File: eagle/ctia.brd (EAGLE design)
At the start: 69.8 x 65.7 mm, 9 parts, among them IC1 IVC102UADAPTOR

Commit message: board/solid works
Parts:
- removed X1, X3, X4, X6: (no value), con-molex:KK-156-2
- removed X2: (no value), con-molex:KK-156-6
- added U$1: CTIA, ctia:CTIA
- added X5: (no value), con-subd:F09HP
- moved R2 22.2 mm to (36.8, 40.6), turned to 180 degrees
- moved R1 14.0 mm to (40.6, 47.0), turned to 180 degrees
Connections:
- removed net N$5: IC1.2, X6.1
- removed net N$6: IC1.10, X1.1
- new net VIN: IC1.2, U$1.P$1
- new net VOUT: IC1.10, X5.8
- net +15V: now also X5.1; no longer X2.6
- net +5V: now also X5.5; no longer X2.4, X2.5
- net -15V: now also X5.4; no longer X2.1
- net GND: now also X5.2, X5.3, X5.9; no longer X1.2, X2.2, X2.3, X3.1, X4.1, X6.2
- net RESET: now also X5.6; no longer X3.2
- net SAMPLE: now also X5.7; no longer X4.2
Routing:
- net N$5: track 38.5 -> 0.00 mm
- net VIN: track 0.00 -> 33.7 mm
- net N$6: track 28.7 -> 0.00 mm
- net VOUT: track 0.00 -> 26.0 mm
- net -15V: track 48.2 -> 24.0 mm, vias 0 -> 1
- net +5V: track 44.0 -> 21.8 mm, vias 0 -> 1
- net RESET: track 38.2 -> 26.2 mm
- net GND: track 0.00 -> 9.92 mm
- net SAMPLE: track 33.3 -> 26.1 mm
- net +15V: track 20.7 -> 24.1 mm
- net N$4: vias 0 -> 1
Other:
- board size 69.8 x 65.7 mm -> 75.2 x 65.7 mm

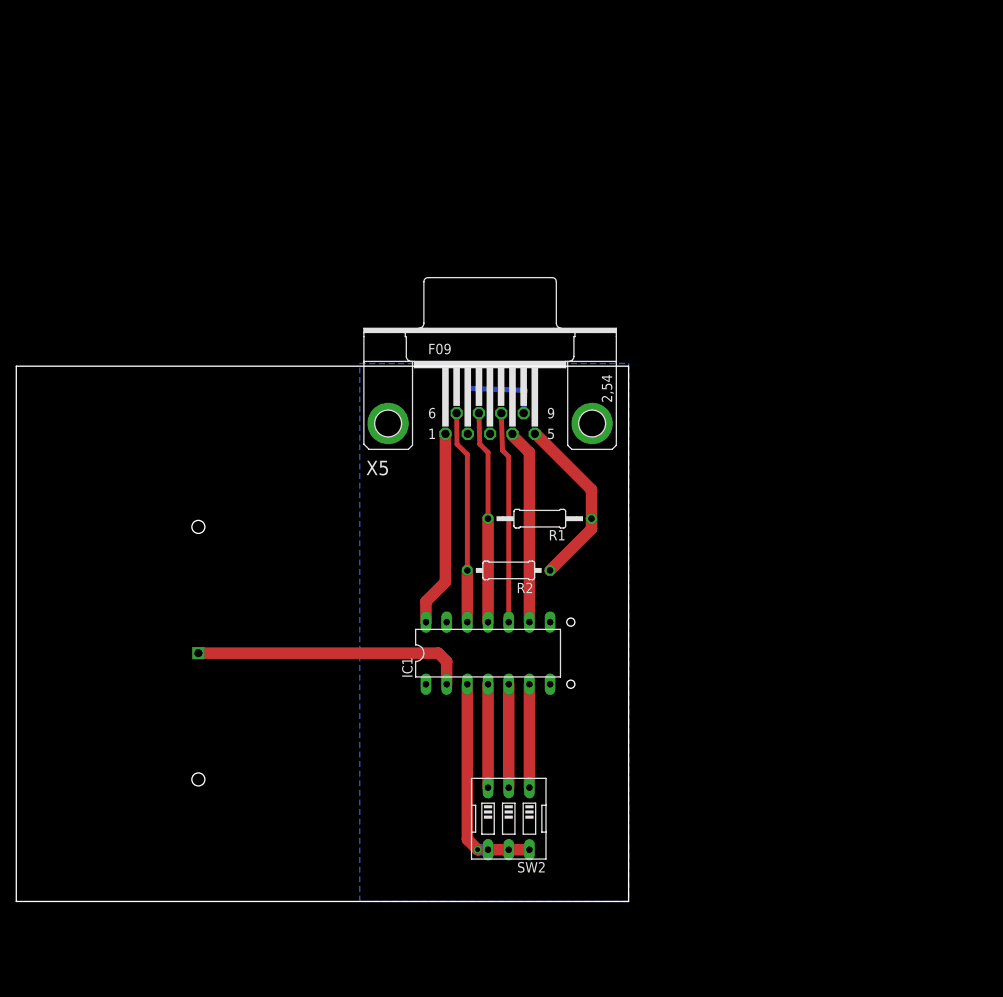
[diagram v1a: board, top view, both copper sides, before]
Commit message: flange alone board for test
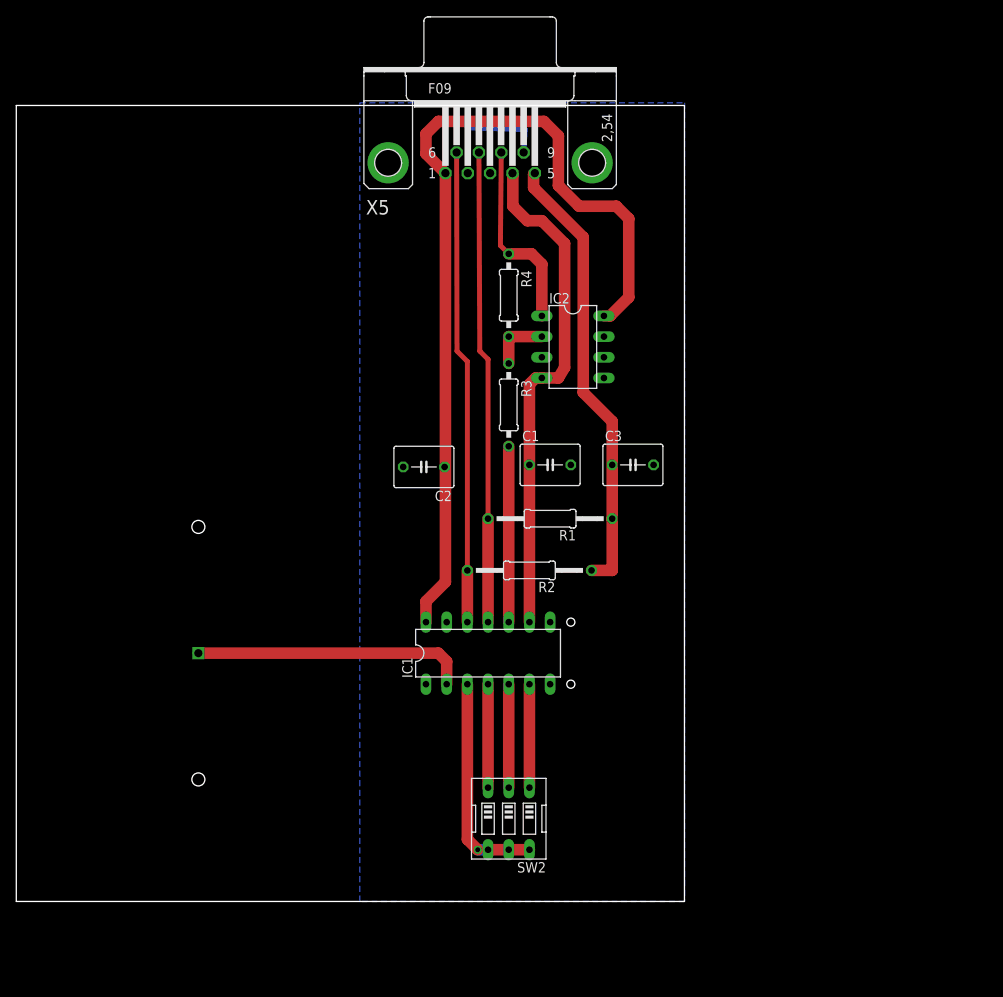
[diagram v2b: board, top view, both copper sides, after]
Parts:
- added C1, C2, C3: 10n, rcl:C050-050X075
- added IC2: LT1352PA, linear-technology:DIL08
- added R3, R4: 10k, resistor:0207/10
- R1: value (none) -> 10k; device resistor:0207/12 -> resistor:0207/15
- R2: value (none) -> 10k; device resistor:0207/10 -> resistor:0207/15
- moved X5 32.0 mm to (34.5, 90.7)
- moved R2 2.54 mm to (39.4, 40.6)
- moved R1 1.27 mm to (41.9, 47.0)
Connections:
- new net N$5: IC1.10, R3.2
- new net N$6: IC2.2, R3.1, R4.2
- net +15V: now also C2.1, IC2.8
- net +5V: now also C3.1
- net -15V: now also C1.1, IC2.4
- net GND: now also C1.2, C3.2, IC2.3
- net VOUT: now also IC2.1, R4.1; no longer IC1.10
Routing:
- net +15V: track 24.1 -> 109.6 mm
- net -15V: track 24.0 -> 62.2 mm
- net +5V: track 21.8 -> 55.4 mm, vias 1 -> 0
- net RESET: track 26.2 -> 58.2 mm
- net SAMPLE: track 26.1 -> 58.1 mm
- net N$5: track 0.00 -> 21.6 mm
- net N$6: track 0.00 -> 7.37 mm
- net VOUT: track 26.0 -> 23.8 mm
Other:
- board size 75.2 x 65.7 mm -> 82 x 97.7 mm

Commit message: zener protect
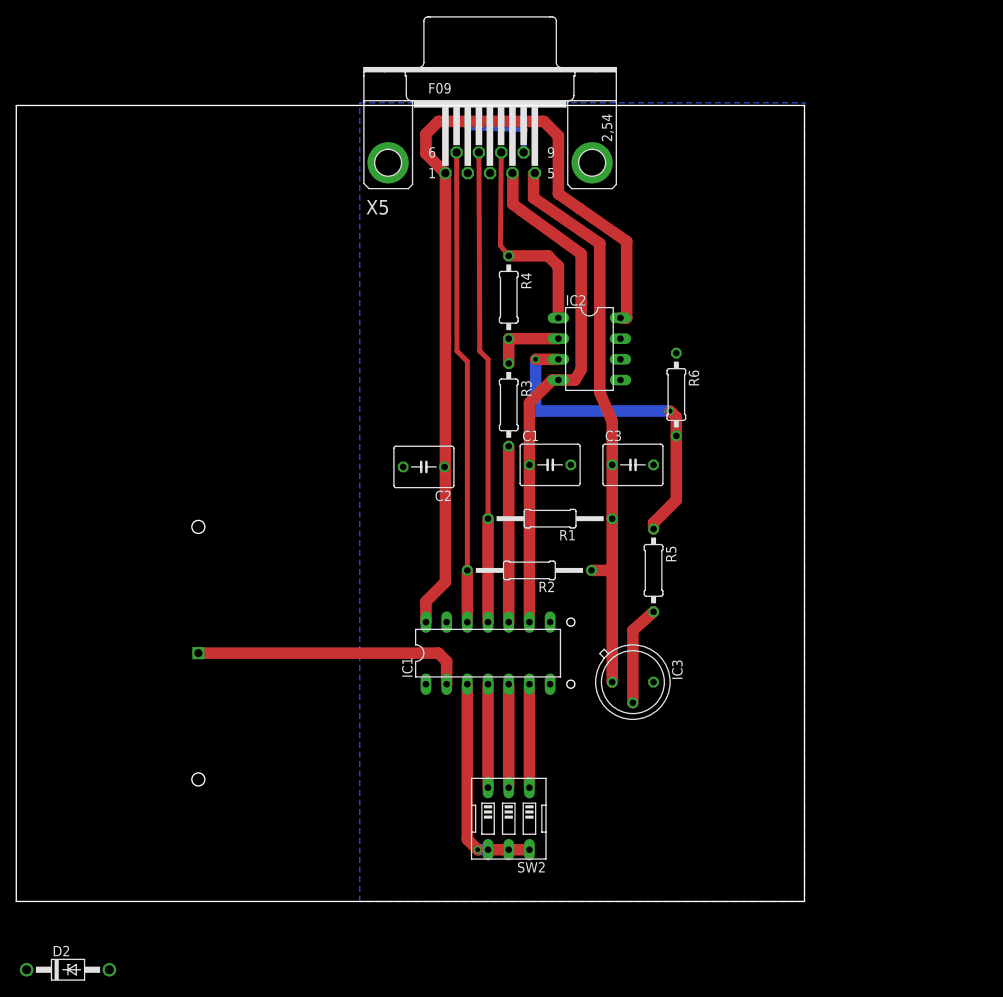
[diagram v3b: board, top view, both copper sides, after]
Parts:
- added D2: (no value), diode:DO41Z10
- added IC3: AD580H, linear:TO39
- added R5: 1.5M, resistor:0207/10
- added R6: 10k, resistor:0207/10
- R4: value 10k -> 1.5M
- moved IC2 2.05 mm to (46.7, 67.8)
- moved R4 0.25 mm to (36.8, 74.2)
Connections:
- new net N$7: IC2.3, R5.1, R6.2
- new net N$8: IC3.2, R5.2
- net +5V: now also IC3.1
- net GND: now also C2.2, D2.A, IC3.3, R6.1; no longer IC2.3
- net VOUT: now also D2.C
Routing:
- net N$7: track 0.00 -> 41.6 mm, vias 0 -> 2
- net +5V: track 55.4 -> 69.7 mm
- net N$8: track 0.00 -> 12.3 mm
- net +15V: track 109.6 -> 107.0 mm
- net VOUT: track 23.8 -> 26.0 mm
- net N$6: track 7.37 -> 9.14 mm
- net -15V: track 62.2 -> 63.6 mm
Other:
- board size 82 x 97.7 mm -> 96.8 x 97.7 mm

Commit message: lower noise
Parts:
- added R7: 10k, pot:B64Y
- IC2: value LT1352PA -> OPA27GP; device linear-technology:DIL08 -> linear:DIL08
- R3, R6: value 10k -> 1M
- R4, R5: value 1.5M -> 1M
- moved D2 123.4 mm to (85.6, 59.7), turned to 270 degrees
- moved C3 49.0 mm to (79.0, 12.7)
- moved R6 36.3 mm to (87.1, 41.4), turned to 90 degrees
- moved C1 34.1 mm to (75.9, 54.9)
- moved IC2 28.1 mm to (74.7, 70.6)
- moved IC3 27.0 mm to (79.0, 25.1)
- moved C2 25.2 mm to (50.0, 62.2)
- moved R5 24.4 mm to (79.0, 41.4)
- moved X5 23.7 mm to (58.2, 88.4)
- moved U$1 23.7 mm to (21.3, 37.6)
- moved R4 23.6 mm to (60.5, 73.2)
- moved R3 23.6 mm to (60.5, 60.2)
- moved IC1 23.6 mm to (57.9, 30.5)
- moved R1 23.6 mm to (65.5, 47.0)
- moved R2 23.6 mm to (63.0, 40.6)
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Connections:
- new net N$10: IC2.8, R7.A
- new net N$9: IC2.1, R7.E
- net +15V: now also IC2.7, R7.S; no longer IC2.8
- net VOUT: now also IC2.6; no longer IC2.1
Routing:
- net N$9: track 0.00 -> 25.3 mm
- net VOUT: track 26.0 -> 45.7 mm
- net +15V: track 107.0 -> 122.1 mm
- net +5V: track 69.7 -> 83.9 mm
- net N$10: track 0.00 -> 10.4 mm
- net -15V: track 63.6 -> 70.8 mm
- net N$7: track 41.6 -> 35.4 mm, vias 2 -> 0
- net N$6: track 9.14 -> 14.8 mm
- net VIN: track 33.7 -> 38.3 mm
- net RESET: track 58.2 -> 55.9 mm
- net SAMPLE: track 58.1 -> 55.8 mm
- net N$8: track 12.3 -> 13.7 mm
- net N$5: track 21.6 -> 20.8 mm
- net N$4: vias 1 -> 0
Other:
- board size 96.8 x 97.7 mm -> 95.2 x 95.2 mm
